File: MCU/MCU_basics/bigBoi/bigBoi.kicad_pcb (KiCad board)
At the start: 4 copper layers, 70 x 70 mm, 97 parts, among them IC1 BMP390, J1 Conn_Coaxial, J2 Conn_Coaxial, J3 DM3AT-SF-PEJM5_40_, J4 Conn_01x05, J5 Conn_01x04, J6 Conn_01x06, J7 USB_B_Micro, SW1 Boot Switch, U1 STM32F469NIHx, U2 LT1963AxST-3.3, U3 SX1276, U4 PE4259, U5 MIA-M10Q, U6 BNO086, U7 USBLC6-2SC6, Y1 8MHz, Y2 32MHz, Y3 32kHz

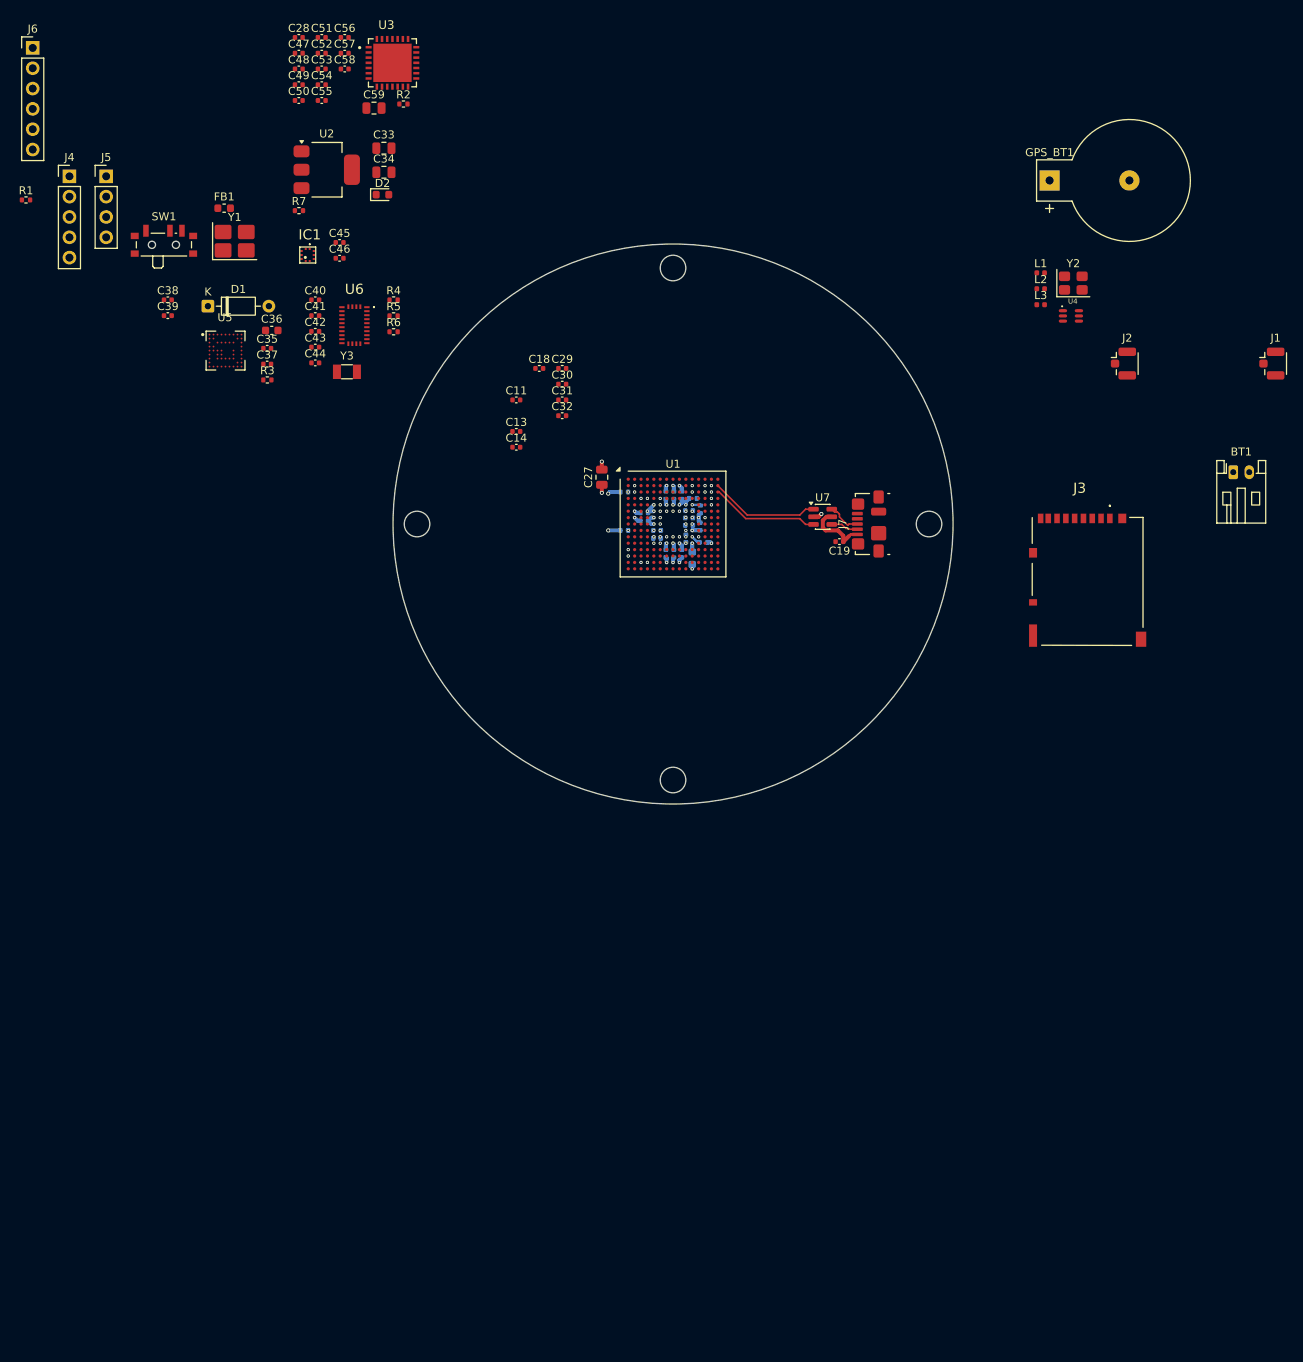
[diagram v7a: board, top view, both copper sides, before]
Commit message: Layout kategorier
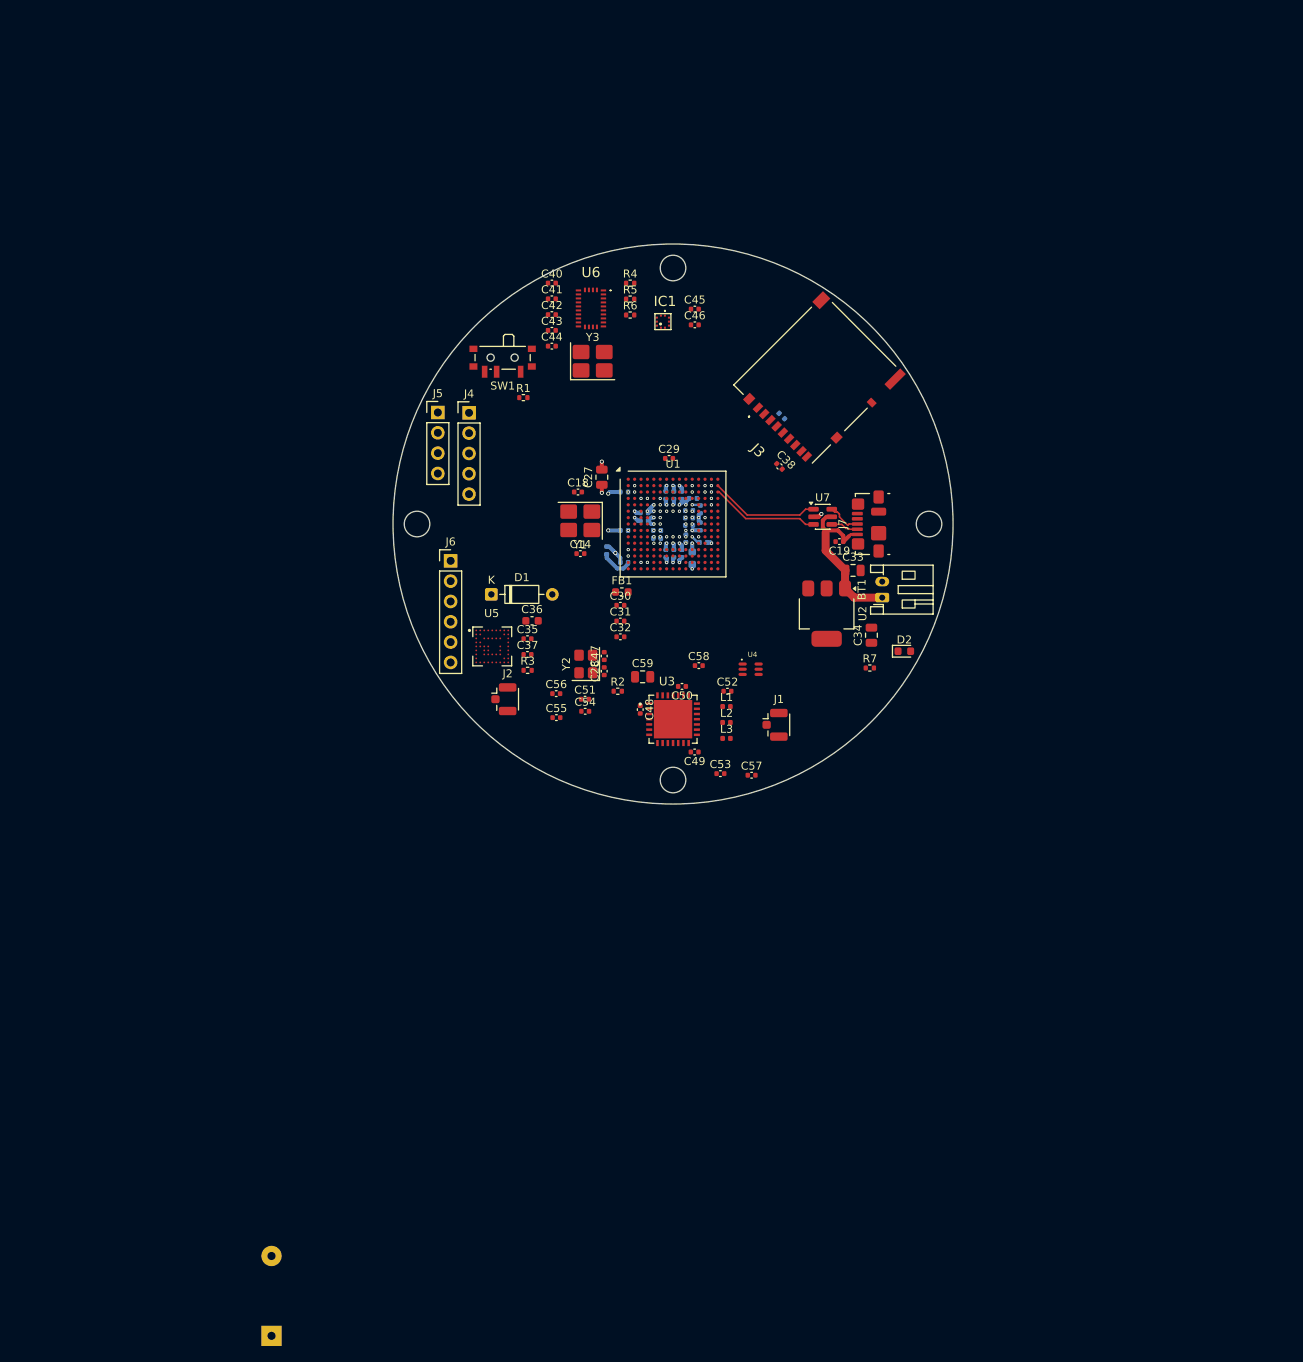
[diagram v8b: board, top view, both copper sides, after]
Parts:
- C11, C13, C39, GPS_BT1: moved to B.Cu
- Y3: footprint Crystal:Crystal_SMD_3215-2Pin_3.2x1.5mm -> Crystal:Crystal_SMD_3225-4Pin_3.2x2.5mm_HandSoldering
- moved GPS_BT1 174.1 mm to (57.8, 201.5), turned to 90 degrees
- moved C57 103.6 mm to (117.8, 131.4)
- moved C53 101.2 mm to (113.9, 131.2)
- moved C49 97.0 mm to (110.7, 128.5), turned to 180 degrees
- moved C52 94.5 mm to (114.8, 120.9)
- moved R7 91.4 mm to (132.6, 118.0)
- moved C48 90.7 mm to (103.9, 123.2), turned to -90 degrees
- moved U3 89.2 mm to (108.0, 124.4)
- moved C51 89.0 mm to (97.0, 121.9)
- moved J2 88.1 mm to (87.3, 121.9)
- moved C28 87.9 mm to (99.4, 118.4), turned to 90 degrees
- moved C50 87.5 mm to (109.1, 120.3), turned to 180 degrees
- moved C58 86.7 mm to (111.2, 117.7)
- moved D2 86.7 mm to (136.9, 115.9)
- moved C56 86.2 mm to (93.4, 121.2)
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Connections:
- C38 pad 2: <NO NET> -> GND
- C39 pad 2: <NO NET> -> GND
- Y3 pad 2: /BNO086/XOUT32BNO086 -> GND
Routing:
- net VBUS: track 8.04 -> 21.2 mm
- net Net-(U1-VREF+): track 0.00 -> 4.10 mm
- net +3.3V: track 13.5 -> 16.6 mm, vias 22 -> 23
